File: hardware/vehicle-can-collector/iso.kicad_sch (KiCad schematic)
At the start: 15 parts, among them Q901 2N7002, Q902 2N7002, Q903 MMBT3904, Q904 2N7002, U901 AS2333Q

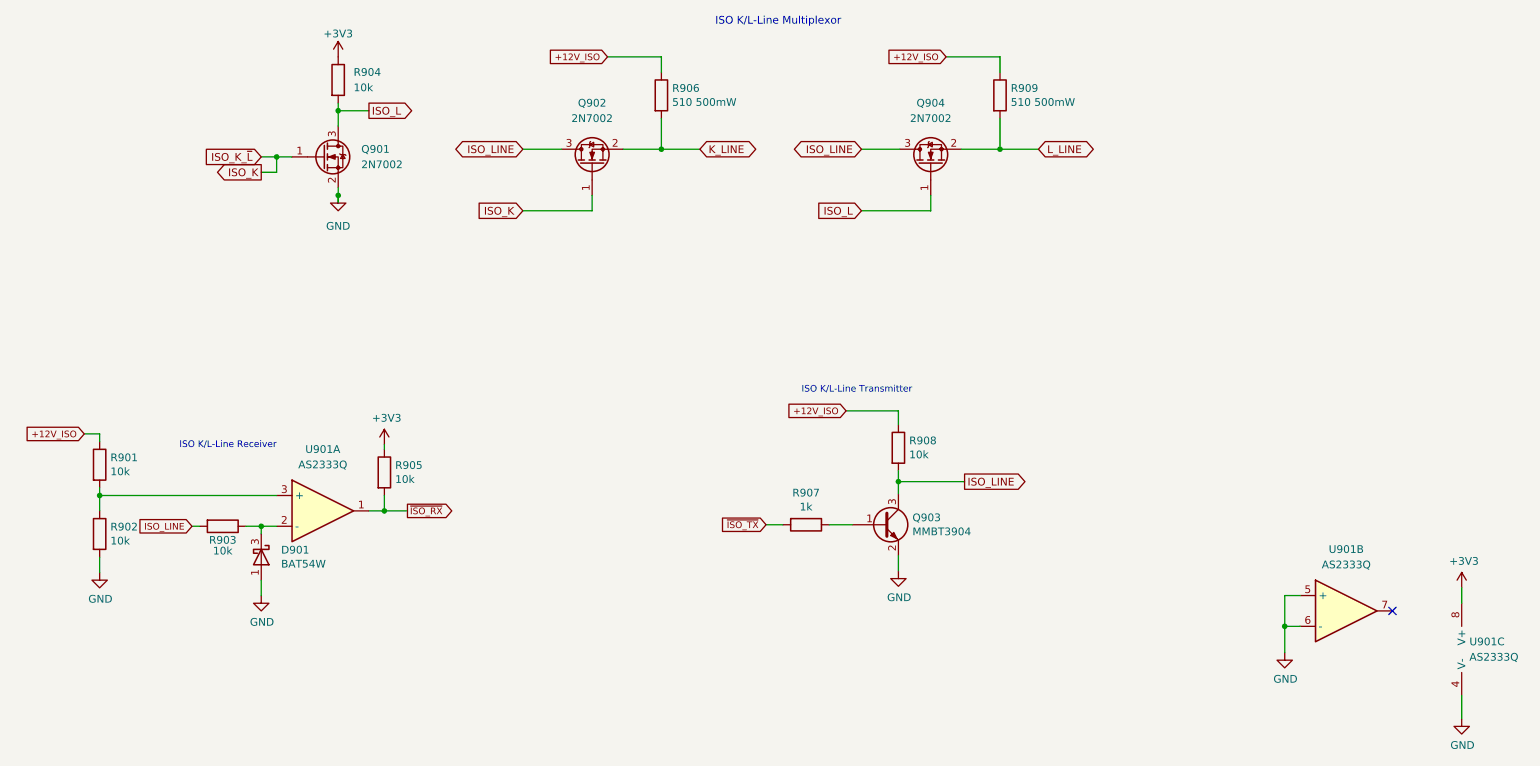
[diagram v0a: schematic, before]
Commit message: Added decoupling, more LEDs, update dts
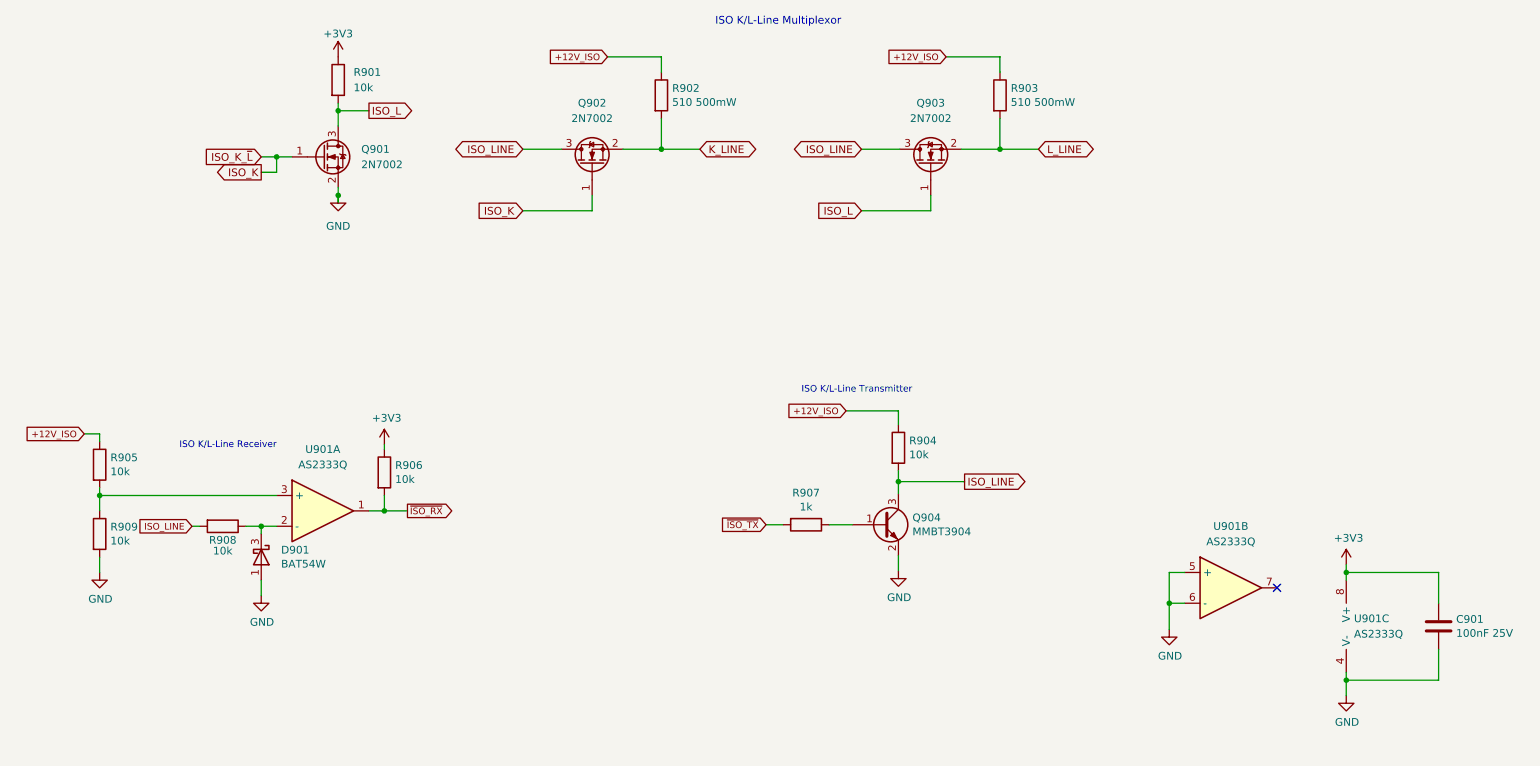
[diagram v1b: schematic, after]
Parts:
- added C901: 100nF 25V, symbol Device:C
- renumbered Q904 to Q903, Q903 to Q904, R904 to R901, R906 to R902, R909 to R903, R908 to R904, R901 to R905, R905 to R906, R903 to R908, R902 to R909
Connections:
- net +3V3: now also C901.2
- net GND: now also C901.1
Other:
- company: (none) -> Gavin Hurlbut
- title: (none) -> Vehicle CAN Collector
- moved on the sheet: U901B, U901C

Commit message: Added footprints, tossed all footprints onto PCB
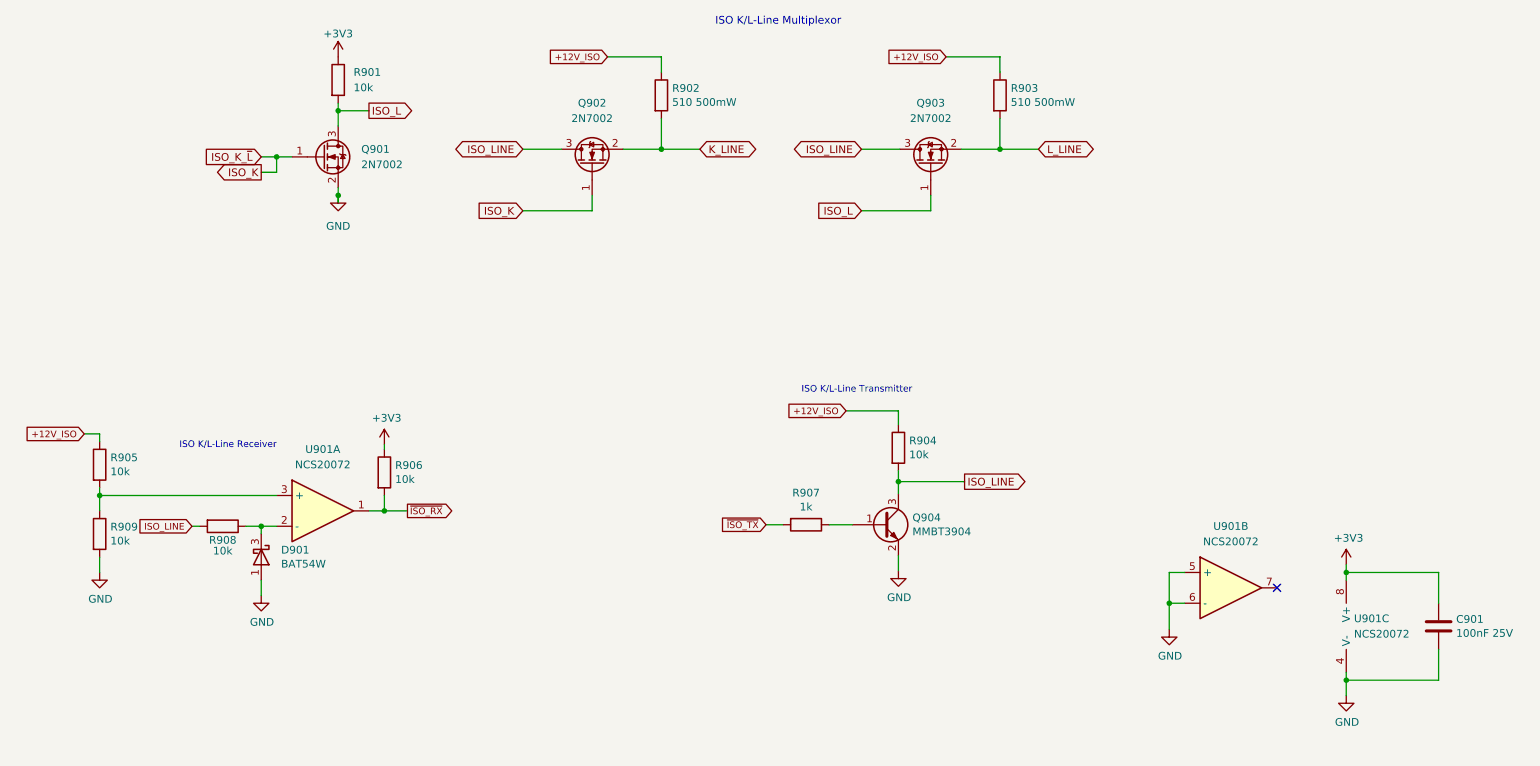
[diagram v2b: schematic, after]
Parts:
- C901: footprint (none) -> Capacitor_SMD:C_0805_2012Metric_Pad1.18x1.45mm_HandSolder
- R901, R904, R905, R906, R907, R908, R909: footprint (none) -> Resistor_SMD:R_0805_2012Metric_Pad1.20x1.40mm_HandSolder
- R902, R903: footprint (none) -> Resistor_SMD:R_1210_3225Metric_Pad1.30x2.65mm_HandSolder
- U901: value AS2333Q -> NCS20072; footprint Package_SO:SOIC-8_3.9x4.9mm_P1.27mm -> Package_SO:TSSOP-8_4.4x3mm_P0.65mm
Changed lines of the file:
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@@
     (property "Reference" "R908" (id 0) (at 62.23 124.206 90))
     (property "Value" "10k" (id 1) (at 62.23 125.984 90))
-    (property "Footprint" "" (id 2) (at 62.23 120.142 90)
+    (property "Footprint" "Resistor_SMD:R_0805_2012Metric_Pad1.20x1.40mm_HandSolder" (id 2) (at 62.23 120.142 90)
       (effects (font (size 1.27 1.27)) hide)
     )
@@
     (property "Reference" "R907" (id 0) (at 158.496 116.4082 90))
     (property "Value" "1k" (id 1) (at 158.496 118.7196 90))
-    (property "Footprint" "" (id 2) (at 158.496 119.888 90)
+    (property "Footprint" "Resistor_SMD:R_0805_2012Metric_Pad1.20x1.40mm_HandSolder" (id 2) (at 158.496 119.888 90)
       (effects (font (size 1.27 1.27)) hide)
     )
@@
       (effects (font (size 1.27 1.27)) (justify left))
     )
-    (property "Footprint" "" (id 2) (at 188.722 50.8 90)
+    (property "Footprint" "Resistor_SMD:R_1210_3225Metric_Pad1.30x2.65mm_HandSolder" (id 2) (at 188.722 50.8 90)
       (effects (font (size 1.27 1.27)) hide)
     )
@@
       (effects (font (size 1.27 1.27)) (justify left))
     )
-    (property "Footprint" "" (id 2) (at 40.132 123.19 90)
+    (property "Footprint" "Resistor_SMD:R_0805_2012Metric_Pad1.20x1.40mm_HandSolder" (id 2) (at 40.132 123.19 90)
       (effects (font (size 1.27 1.27)) hide)
     )
@@
       (effects (font (size 1.27 1.27)) (justify left))
     )
-    (property "Footprint" "" (id 2) (at 171.958 108.966 90)
+    (property "Footprint" "Resistor_SMD:R_0805_2012Metric_Pad1.20x1.40mm_HandSolder" (id 2) (at 171.958 108.966 90)
       (effects (font (size 1.27 1.27)) hide)
     )
@@
     (in_bom yes) (on_board yes) (fields_autoplaced)
     (property "Reference" "U901" (id 0) (at 78.74 109.22 0))
-    (property "Value" "AS2333Q" (id 1) (at 78.74 111.76 0))
-    (property "Footprint" "Package_SO:SOIC-8_3.9x4.9mm_P1.27mm" (id 2) (at 78.74 119.38 0)
-      (effects (font (size 1.27 1.27)) hide)
+    (property "Value" "NCS20072" (id 1) (at 78.74 111.76 0))
+    (property "Footprint" "Package_SO:TSSOP-8_4.4x3mm_P0.65mm" (id 2) (at 78.74 119.38 0)
+      (effects (font (size 0 0)) hide)
     )
     (property "Datasheet" "~" (id 3) (at 78.74 119.38 0)
@@
       (effects (font (size 1.27 1.27)) (justify left))
     )
-    (property "Footprint" "" (id 2) (at 132.842 50.8 90)
+    (property "Footprint" "Resistor_SMD:R_1210_3225Metric_Pad1.30x2.65mm_HandSolder" (id 2) (at 132.842 50.8 90)
       (effects (font (size 1.27 1.27)) hide)
     )
@@
       (effects (font (size 1.27 1.27)) (justify right))
     )
-    (property "Footprint" "" (id 2) (at 261.9248 134.62 0)
+    (property "Footprint" "Capacitor_SMD:C_0805_2012Metric_Pad1.18x1.45mm_HandSolder" (id 2) (at 261.9248 134.62 0)
       (effects (font (size 1.27 1.27)) hide)
     )
@@
     (in_bom yes) (on_board yes) (fields_autoplaced)
     (property "Reference" "U901" (id 0) (at 228.6 121.92 0))
-    (property "Value" "AS2333Q" (id 1) (at 228.6 124.46 0))
-    (property "Footprint" "Package_SO:SOIC-8_3.9x4.9mm_P1.27mm" (id 2) (at 228.6 132.08 0)
+    (property "Value" "NCS20072" (id 1) (at 228.6 124.46 0))
+    (property "Footprint" "Package_SO:TSSOP-8_4.4x3mm_P0.65mm" (id 2) (at 228.6 132.08 0)
       (effects (font (size 1.27 1.27)) hide)
     )
@@
       (effects (font (size 1.27 1.27)) (justify left))
     )
-    (property "Footprint" "" (id 2) (at 40.132 111.76 90)
+    (property "Footprint" "Resistor_SMD:R_0805_2012Metric_Pad1.20x1.40mm_HandSolder" (id 2) (at 40.132 111.76 90)
       (effects (font (size 1.27 1.27)) hide)
     )
@@
       (effects (font (size 1.27 1.27)) (justify left))
     )
-    (property "Footprint" "" (id 2) (at 87.122 113.03 90)
+    (property "Footprint" "Resistor_SMD:R_0805_2012Metric_Pad1.20x1.40mm_HandSolder" (id 2) (at 87.122 113.03 90)
       (effects (font (size 1.27 1.27)) hide)
     )
@@
       (effects (font (size 1.27 1.27)) (justify left))
     )
-    (property "Value" "AS2333Q" (id 1) (at 248.92 139.6999 0)
-      (effects (font (size 1.27 1.27)) (justify left))
-    )
-    (property "Footprint" "Package_SO:SOIC-8_3.9x4.9mm_P1.27mm" (id 2) (at 250.19 138.43 0)
+    (property "Value" "NCS20072" (id 1) (at 248.92 139.6999 0)
+      (effects (font (size 1.27 1.27)) (justify left))
+    )
+    (property "Footprint" "Package_SO:TSSOP-8_4.4x3mm_P0.65mm" (id 2) (at 250.19 138.43 0)
       (effects (font (size 1.27 1.27)) hide)
     )
@@
       (effects (font (size 1.27 1.27)) (justify left))
     )
-    (property "Footprint" "" (id 2) (at 79.502 48.26 90)
-      (effects (font (size 1.27 1.27)) hide)
-    )
+    (property "Footprint" "Resistor_SMD:R_0805_2012Metric_Pad1.20x1.40mm_HandSolder" (id 2) (at 79.502 48.26 90)
+      (effects (font (size 1.27 1.27)) hide)
+    )
